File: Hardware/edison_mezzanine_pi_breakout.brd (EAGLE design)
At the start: 30.5 x 87.6 mm, 47 parts, among them U1 PCA9306, U2 EDISON_CONNECTOR_FULLMOUNTING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, U3 EDISON_CONNECTOR_FULLHEADER, U4 TPS62065, U5 MIC5219 3.3V

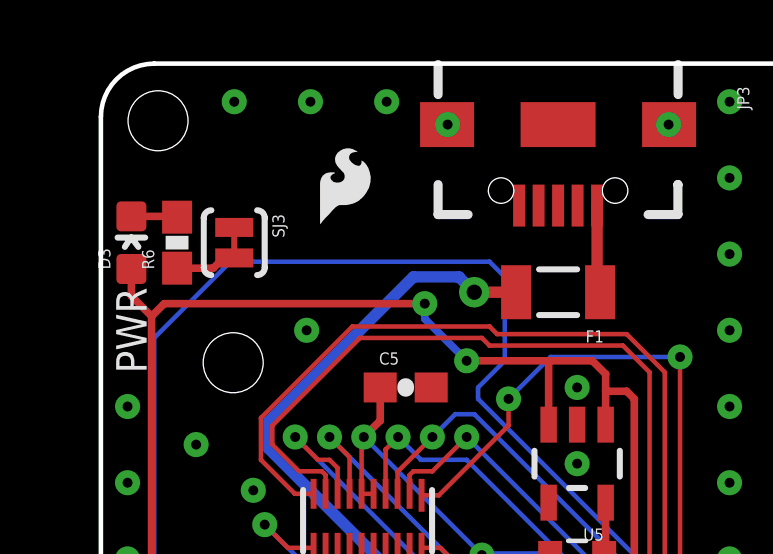
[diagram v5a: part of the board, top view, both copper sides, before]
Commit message: Added LED EN to silk. Enlargened section headings on schem.
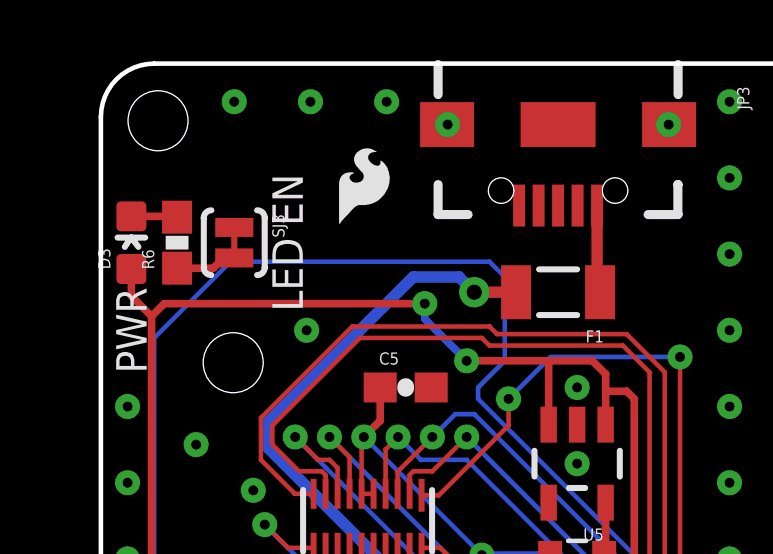
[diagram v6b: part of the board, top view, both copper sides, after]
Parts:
- moved LOGO3 0.63 mm to (7.62, 38.7)
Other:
- board text added: "LED EN"
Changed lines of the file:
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@@
 <setting verticaltext="up"/>
 </settings>
-<grid distance="0.01" unitdist="inch" unit="inch" style="dots" multiple="1" display="yes" altdistance="0.005" altunitdist="inch" altunit="inch"/>
+<grid distance="0.05" unitdist="inch" unit="inch" style="dots" multiple="1" display="yes" altdistance="0.025" altunitdist="inch" altunit="inch"/>
 <layers>
 <layer number="1" name="Top" color="4" fill="1" visible="yes" active="yes"/>
@@
 <text x="1.524" y="9.398" size="1.016" layer="21" font="vector" ratio="15" rot="R90">POWER</text>
 <text x="29.083" y="29.21" size="1.27" layer="22" font="vector" ratio="15" rot="MR90" align="center">Pi Breakout</text>
+<text x="6.223" y="38.481" size="1.016" layer="21" font="vector" ratio="15" rot="R90" align="center">LED EN</text>
 </plain>
 <attributes>
@@
 <attribute name="PROD_ID" value="RES-07861" x="3.81" y="12.065" size="1.778" layer="27" rot="R180" display="off"/>
 </element>
-<element name="LOGO3" library="SparkFun-Aesthetics" package="SFE_LOGO_FLAME_.1" value="SFE_LOGO_FLAME.1_INCH" x="6.985" y="38.735"/>
+<element name="LOGO3" library="SparkFun-Aesthetics" package="SFE_LOGO_FLAME_.1" value="SFE_LOGO_FLAME.1_INCH" x="7.62" y="38.735"/>
 </elements>
 <signals>
